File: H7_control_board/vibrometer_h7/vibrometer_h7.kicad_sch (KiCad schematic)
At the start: 0 parts

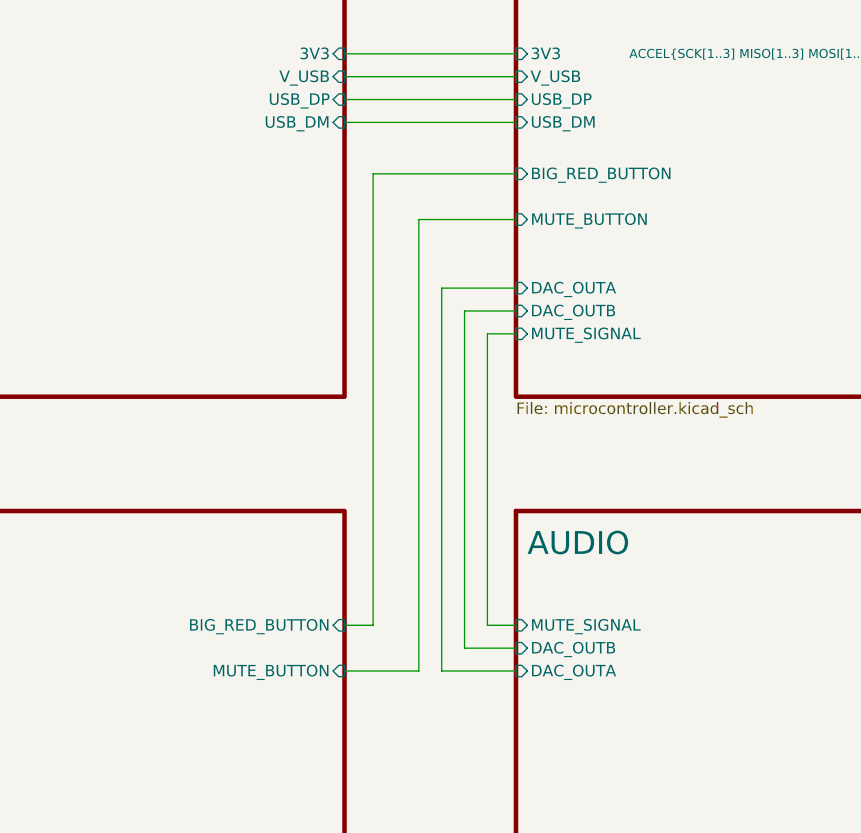
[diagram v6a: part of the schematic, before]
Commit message: worked on power supply filtering
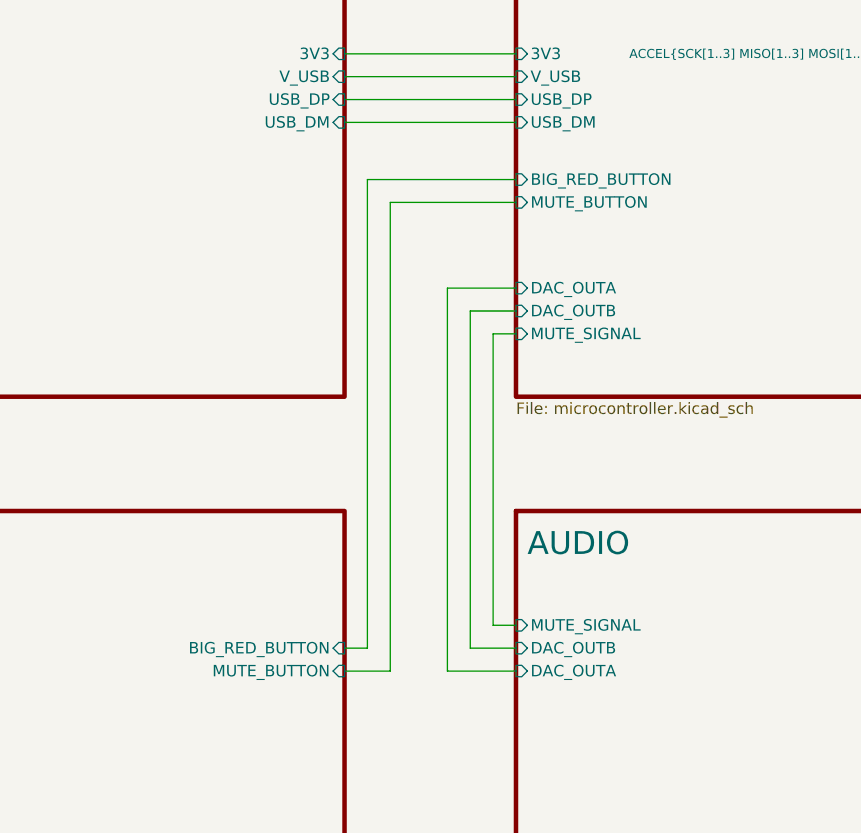
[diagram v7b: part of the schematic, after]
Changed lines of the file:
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@@
 	(wire
 		(pts
-			(xy 108.585 79.375) (xy 108.585 116.84)
-		)
-		(stroke
-			(width 0)
-			(type default)
-		)
-	)
-	(wire
-		(pts
-			(xy 114.3 76.835) (xy 106.045 76.835)
-		)
-		(stroke
-			(width 0)
-			(type default)
-		)
-	)
-	(wire
-		(pts
-			(xy 108.585 116.84) (xy 114.3 116.84)
+			(xy 109.22 79.375) (xy 109.22 116.84)
+		)
+		(stroke
+			(width 0)
+			(type default)
+		)
+	)
+	(wire
+		(pts
+			(xy 114.3 76.835) (xy 106.68 76.835)
+		)
+		(stroke
+			(width 0)
+			(type default)
+		)
+	)
+	(wire
+		(pts
+			(xy 109.22 116.84) (xy 114.3 116.84)
 		)
 		(stroke
@@
 	(wire
 		(pts
-			(xy 98.425 64.135) (xy 98.425 114.3)
-		)
-		(stroke
-			(width 0)
-			(type default)
-		)
-	)
-	(wire
-		(pts
-			(xy 111.125 114.3) (xy 114.3 114.3)
-		)
-		(stroke
-			(width 0)
-			(type default)
-		)
-	)
-	(wire
-		(pts
-			(xy 103.505 69.215) (xy 114.3 69.215)
-		)
-		(stroke
-			(width 0)
-			(type default)
-		)
-	)
-	(wire
-		(pts
-			(xy 103.505 119.38) (xy 95.25 119.38)
-		)
-		(stroke
-			(width 0)
-			(type default)
-		)
-	)
-	(wire
-		(pts
-			(xy 98.425 114.3) (xy 95.25 114.3)
-		)
-		(stroke
-			(width 0)
-			(type default)
-		)
-	)
-	(wire
-		(pts
-			(xy 114.3 64.135) (xy 98.425 64.135)
+			(xy 97.79 64.77) (xy 97.79 116.84)
+		)
+		(stroke
+			(width 0)
+			(type default)
+		)
+	)
+	(wire
+		(pts
+			(xy 111.76 114.3) (xy 114.3 114.3)
+		)
+		(stroke
+			(width 0)
+			(type default)
+		)
+	)
+	(wire
+		(pts
+			(xy 100.33 67.31) (xy 114.3 67.31)
+		)
+		(stroke
+			(width 0)
+			(type default)
+		)
+	)
+	(wire
+		(pts
+			(xy 100.33 119.38) (xy 95.25 119.38)
+		)
+		(stroke
+			(width 0)
+			(type default)
+		)
+	)
+	(wire
+		(pts
+			(xy 97.79 116.84) (xy 95.25 116.84)
+		)
+		(stroke
+			(width 0)
+			(type default)
+		)
+	)
+	(wire
+		(pts
+			(xy 114.3 64.77) (xy 97.79 64.77)
 		)
 		(stroke
@@
 	(wire
 		(pts
-			(xy 106.045 76.835) (xy 106.045 119.38)
+			(xy 106.68 76.835) (xy 106.68 119.38)
 		)
 		(stroke
@@
 	(wire
 		(pts
-			(xy 114.3 79.375) (xy 108.585 79.375)
-		)
-		(stroke
-			(width 0)
-			(type default)
-		)
-	)
-	(wire
-		(pts
-			(xy 114.3 81.915) (xy 111.125 81.915)
-		)
-		(stroke
-			(width 0)
-			(type default)
-		)
-	)
-	(wire
-		(pts
-			(xy 106.045 119.38) (xy 114.3 119.38)
-		)
-		(stroke
-			(width 0)
-			(type default)
-		)
-	)
-	(wire
-		(pts
-			(xy 103.505 69.215) (xy 103.505 119.38)
-		)
-		(stroke
-			(width 0)
-			(type default)
-		)
-	)
-	(wire
-		(pts
-			(xy 111.125 81.915) (xy 111.125 114.3)
+			(xy 114.3 79.375) (xy 109.22 79.375)
+		)
+		(stroke
+			(width 0)
+			(type default)
+		)
+	)
+	(wire
+		(pts
+			(xy 114.3 81.915) (xy 111.76 81.915)
+		)
+		(stroke
+			(width 0)
+			(type default)
+		)
+	)
+	(wire
+		(pts
+			(xy 106.68 119.38) (xy 114.3 119.38)
+		)
+		(stroke
+			(width 0)
+			(type default)
+		)
+	)
+	(wire
+		(pts
+			(xy 100.33 67.31) (xy 100.33 119.38)
+		)
+		(stroke
+			(width 0)
+			(type default)
+		)
+	)
+	(wire
+		(pts
+			(xy 111.76 81.915) (xy 111.76 114.3)
 		)
 		(stroke
@@
 		)
 		(pin "BIG_RED_BUTTON" input
-			(at 114.3 64.135 180)
+			(at 114.3 64.77 180)
 			(effects
 				(font
@@
 		)
 		(pin "MUTE_BUTTON" input
-			(at 114.3 69.215 180)
+			(at 114.3 67.31 180)
 			(effects
 				(font
@@
 		)
 		(pin "BIG_RED_BUTTON" input
-			(at 95.25 114.3 0)
-			(effects
-				(font
+			(at 95.25 116.84 0)
+			(effects
+				(font

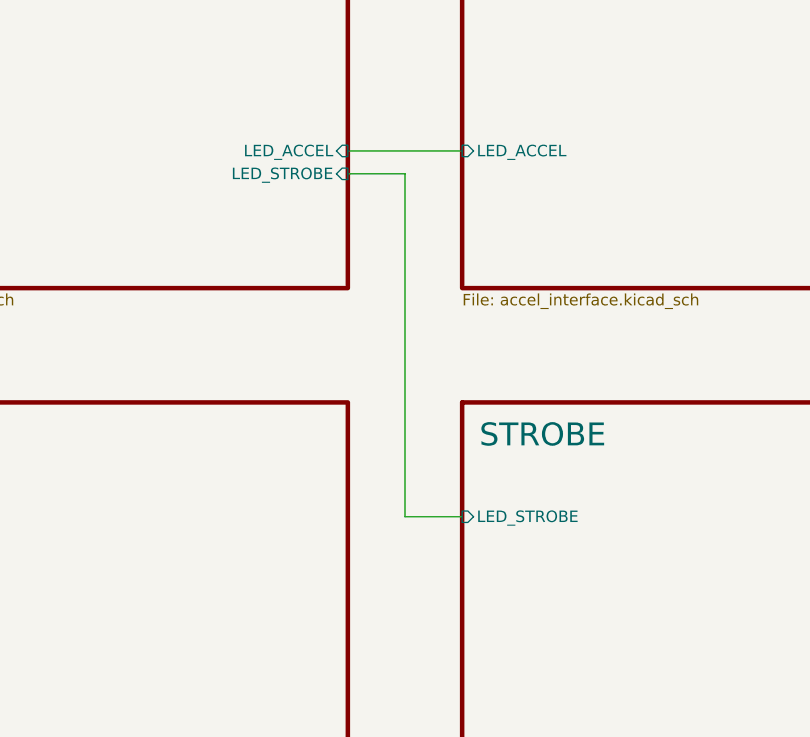
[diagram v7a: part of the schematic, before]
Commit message: first pass at board routing
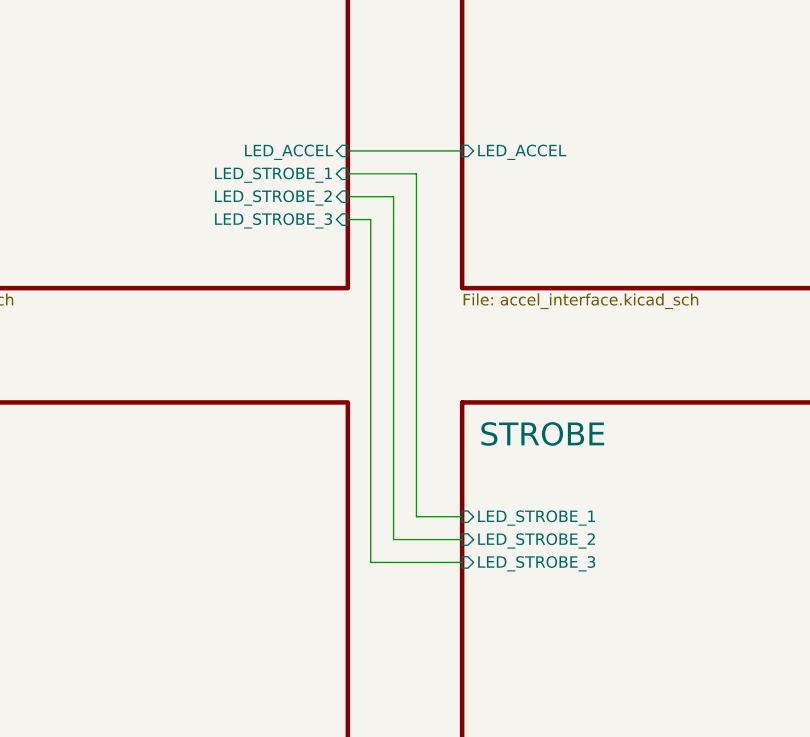
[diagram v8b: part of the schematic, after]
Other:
- sheet MCU ports: added LED_STROBE_1, LED_STROBE_2, LED_STROBE_3; removed LED_STROBE
- sheet STROBE ports: added LED_STROBE_1, LED_STROBE_2, LED_STROBE_3; removed LED_STROBE
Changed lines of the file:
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@@
 	(wire
 		(pts
-			(xy 184.15 114.3) (xy 190.5 114.3)
+			(xy 185.42 114.3) (xy 190.5 114.3)
+		)
+		(stroke
+			(width 0)
+			(type default)
+		)
+	)
+	(wire
+		(pts
+			(xy 182.88 78.74) (xy 182.88 116.84)
 		)
 		(stroke
@@
 	(wire
 		(pts
+			(xy 177.8 81.28) (xy 180.34 81.28)
+		)
+		(stroke
+			(width 0)
+			(type default)
+		)
+	)
+	(wire
+		(pts
 			(xy 100.33 67.31) (xy 114.3 67.31)
 		)
@@
 	(wire
 		(pts
-			(xy 184.15 76.2) (xy 184.15 114.3)
-		)
-		(stroke
-			(width 0)
-			(type default)
-		)
-	)
-	(wire
-		(pts
-			(xy 177.8 76.2) (xy 184.15 76.2)
+			(xy 185.42 76.2) (xy 185.42 114.3)
+		)
+		(stroke
+			(width 0)
+			(type default)
+		)
+	)
+	(wire
+		(pts
+			(xy 177.8 76.2) (xy 185.42 76.2)
 		)
 		(stroke
@@
 	(wire
 		(pts
+			(xy 182.88 116.84) (xy 190.5 116.84)
+		)
+		(stroke
+			(width 0)
+			(type default)
+		)
+	)
+	(wire
+		(pts
 			(xy 95.25 55.88) (xy 114.3 55.88)
 		)
@@
 	(wire
 		(pts
+			(xy 177.8 78.74) (xy 182.88 78.74)
+		)
+		(stroke
+			(width 0)
+			(type default)
+		)
+	)
+	(wire
+		(pts
+			(xy 180.34 119.38) (xy 190.5 119.38)
+		)
+		(stroke
+			(width 0)
+			(type default)
+		)
+	)
+	(wire
+		(pts
 			(xy 114.3 79.375) (xy 109.22 79.375)
 		)
@@
 		(pts
 			(xy 114.3 81.915) (xy 111.76 81.915)
+		)
+		(stroke
+			(width 0)
+			(type default)
+		)
+	)
+	(wire
+		(pts
+			(xy 180.34 81.28) (xy 180.34 119.38)
 		)
 		(stroke
@@
 			)
 		)
-		(pin "LED_STROBE" input
-			(at 177.8 76.2 0)
-			(effects
-				(font
-					(size 1.27 1.27)
-				)
-				(justify right)
-			)
-		)
 		(pin "MUTE_BUTTON" input
 			(at 114.3 67.31 180)
@@
 				)
 				(justify left)
+			)
+		)
+		(pin "LED_STROBE_2" input
+			(at 177.8 78.74 0)
+			(effects
+				(font
+					(size 1.27 1.27)
+				)
+				(justify right)
+			)
+		)
+		(pin "LED_STROBE_1" input
+			(at 177.8 76.2 0)
+			(effects
+				(font
+					(size 1.27 1.27)
+				)
+				(justify right)
+			)
+		)
+		(pin "LED_STROBE_3" input
+			(at 177.8 81.28 0)
+			(effects
+				(font
+					(size 1.27 1.27)
+				)
+				(justify right)
 			)
 		)
@@
 			)
 		)
-		(pin "LED_STROBE" input
+		(pin "LED_STROBE_3" input
+			(at 190.5 119.38 180)
+			(effects
+				(font
+					(size 1.27 1.27)
+				)
+				(justify left)
+			)
+		)
+		(pin "LED_STROBE_1" input
 			(at 190.5 114.3 180)
 			(effects
 				(font
+					(size 1.27 1.27)
+				)
+				(justify left)
+			)
+		)
+		(pin "LED_STROBE_2" input
+			(at 190.5 116.84 180)
+			(effects
+				(font
